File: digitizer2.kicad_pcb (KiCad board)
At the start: 6 copper layers, 75 x 100 mm, 206 parts, among them P1 USB_OTG, P2 CONN_01X01, P3 CONN_01X01, T1 ETC1-1-13, T2 ETC1-1-13, U1 XC7A35T, U10 SN65LVDS100DGK, U11 SN65LVDS100DGK, U2 FT2232H, U3 MT41J128M16, U4 ADS5403, U5 LTC3569, U6 TPS79618DCQ, U7 TPS79633DCQ, U8 93LC46BT-I/OT, U9 LM3671MF-3.3, Y1 12MHz

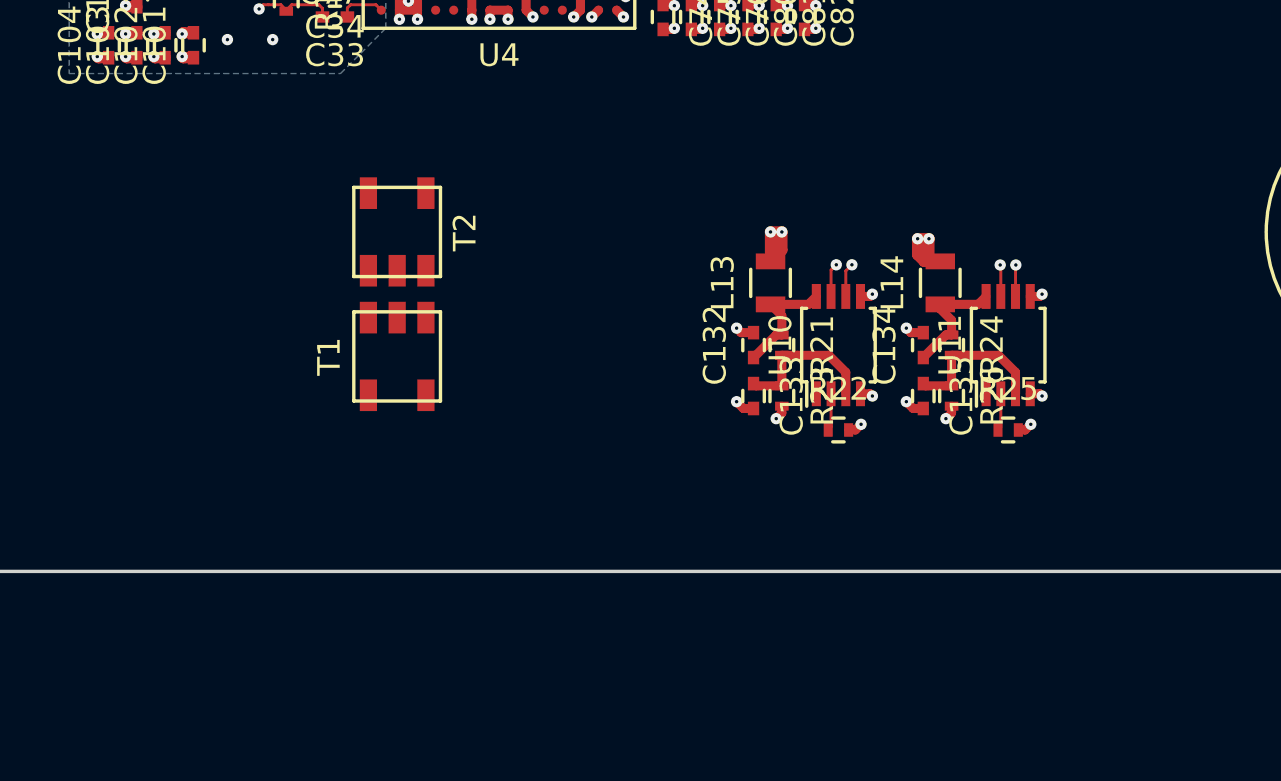
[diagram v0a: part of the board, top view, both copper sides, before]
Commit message: Add SMA connectors
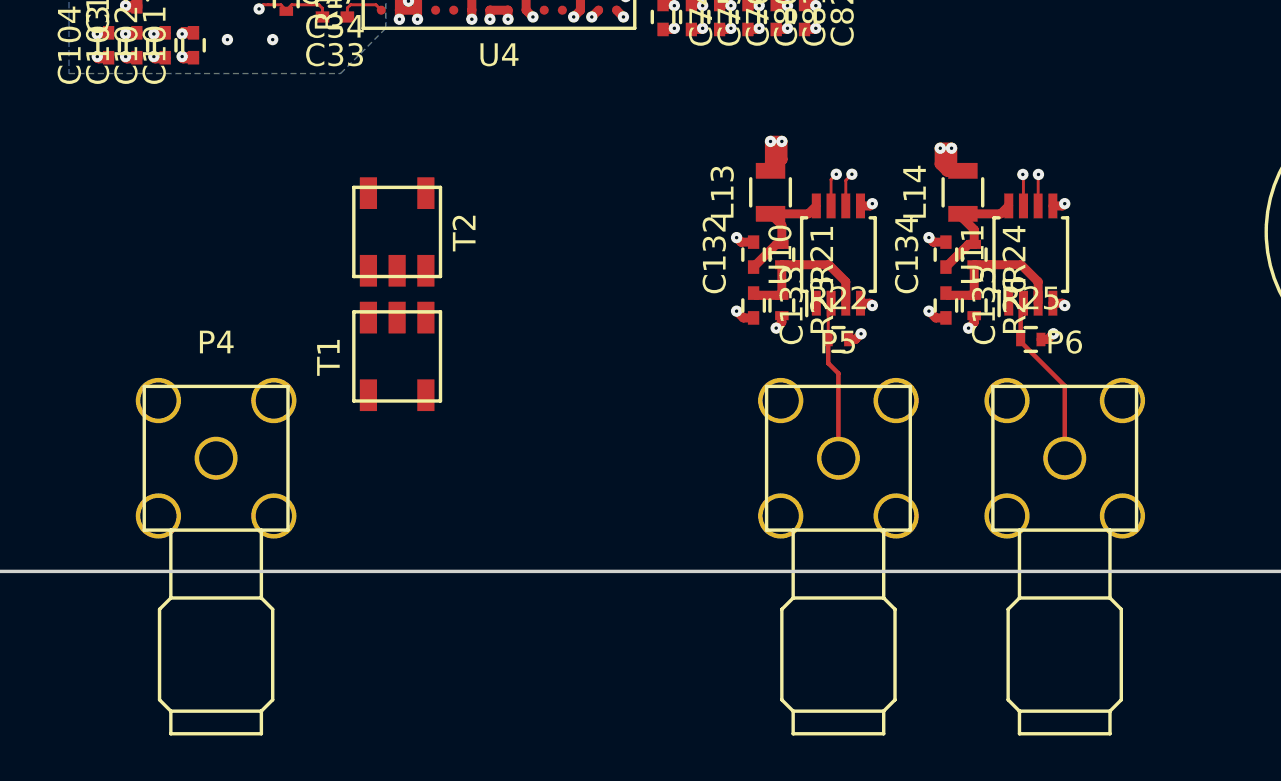
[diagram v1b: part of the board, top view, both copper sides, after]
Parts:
- added P4: SMA, digitizer2_modules:SMA_ANGLE_THT, F.Cu at (147.5, 150.0)
- added P5: SMA, digitizer2_modules:SMA_ANGLE_THT, F.Cu at (175.0, 150.0)
- added P6: SMA, digitizer2_modules:SMA_ANGLE_THT, F.Cu at (185.0, 150.0)
- moved C134 4.12 mm to (179.8, 141.0)
- moved C135 4.12 mm to (179.8, 143.2)
- moved L14 4.12 mm to (180.5, 138.2)
- moved R24 4.12 mm to (181.0, 141.0)
- moved R25 4.12 mm to (183.5, 144.8)
- moved R26 4.12 mm to (181.0, 143.2)
- moved U11 4.12 mm to (183.5, 141.0)
- moved C132 4.00 mm to (171.2, 141.0)
- moved C133 4.00 mm to (171.2, 143.2)
- moved L13 4.00 mm to (172.0, 138.2)
- moved R21 4.00 mm to (172.5, 141.0)
- moved R22 4.00 mm to (175.0, 144.8)
- moved R23 4.00 mm to (172.5, 143.2)
- moved U10 4.00 mm to (175.0, 141.0)
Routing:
- net Net-(P6-Pad1): track 1.65 -> 7.71 mm
- net Net-(P5-Pad1): track 1.65 -> 7.09 mm
- net /DIN2_N: track 51.6 -> 48.0 mm
- net /DIN2_P: track 51.1 -> 48.0 mm
- net /DIN1_P: track 51.0 -> 48.0 mm
- net /DIN1_N: track 51.0 -> 48.0 mm
- net /VDD_ADC_3V3: track 55.6 -> 53.9 mm

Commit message: First digitizer2 release candidate
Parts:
- added C143: 100nF, Capacitors_SMD:C_0402, F.Cu at (140.5, 102.5)
- added C144: 1uF, Capacitors_SMD:C_0402, F.Cu at (158.8, 138.5)
- added C145: 6.8pF NC, Capacitors_SMD:C_0603, F.Cu at (155.0, 152.5)
- added C146: 100nF, Capacitors_SMD:C_0402, F.Cu at (157.5, 138.5)
- added C147: 1uF, Capacitors_SMD:C_0402, F.Cu at (156.2, 138.5)
- added C148: 100nF, Capacitors_SMD:C_0402, F.Cu at (166.0, 133.0)
- added P7: CONN_02X03, Pin_Headers:Pin_Header_Angled_2x03, B.Cu at (140.0, 140.0)
- added P8: CONN_02X03, Pin_Headers:Pin_Header_Angled_2x03, F.Cu at (201.5, 89.5)
- added R29: 0, Resistors_SMD:R_0603, F.Cu at (155.0, 151.0)
- added R30: 0, Resistors_SMD:R_0603, F.Cu at (157.8, 151.0)
- added R31: 50, Resistors_SMD:R_0402, F.Cu at (158.5, 136.8)
- added R32: 0, Resistors_SMD:R_0603, F.Cu at (154.2, 148.5)
- added R33: 50, Resistors_SMD:R_0402, F.Cu at (156.5, 136.8)
- added R34: 100 NC, Resistors_SMD:R_0402, F.Cu at (157.6, 132.0)
- added R35: NC, Resistors_SMD:R_0402, F.Cu at (159.3, 137.9)
- added R36: NC, Resistors_SMD:R_0402, F.Cu at (155.7, 137.9)
- added U12: ASTMLPA-18-100.000MHZ-EJ-E-T, digitizer2_modules:ASTMLPA, F.Cu at (140.5, 100.5)
- moved P5 5.00 mm to (170.0, 150.0)
- moved T2 3.01 mm to (157.5, 142.2)
- moved T1 2.83 mm to (157.5, 147.5)
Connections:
- net /GCLK1_N renamed Net-(U1-PadC4)
- P4 pad 2: Net-(P4-Pad2) -> GND
- U1 pad D4: /GCLK1_P -> /GCLK1
- U1 pad P10: /GCLK2_P -> /GPIO1_P
- U1 pad P11: /GCLK2_N -> /GPIO1_N
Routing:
- net GND: track 242.4 -> 448.9 mm, vias 274 -> 401
- net (no net): track 74.3 -> 0.00 mm, vias 34 -> 0
- net /VDD_ADC_3V3: track 53.9 -> 95.2 mm
- net /GPIO1_N: track 0.00 -> 40.7 mm, vias 0 -> 1
- net /GPIO1_P: track 0.00 -> 40.2 mm, vias 0 -> 1
- net /ADC_VCM: track 0.42 -> 37.2 mm, vias 1 -> 4
- net /INA_BYPASS_P: track 0.00 -> 26.0 mm, vias 0 -> 1
- net /INA_BYPASS_N: track 0.00 -> 25.4 mm, vias 0 -> 1
- net /5V0: track 63.4 -> 38.3 mm
- net /GCLK2_N: track 22.7 -> 0.00 mm, vias 1 -> 0
- net /GCLK2_P: track 22.3 -> 0.00 mm, vias 1 -> 0
- net /GCLK1: track 0.00 -> 16.0 mm, vias 0 -> 2
- net /GCLK1_P: track 12.4 -> 0.00 mm, vias 1 -> 0
- net Net-(U1-PadC4): track 12.4 -> 0.00 mm, vias 1 -> 0
- net /ADC_INA_N: track 0.00 -> 8.35 mm
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- added copper zone on B.Cu, net GND
- added copper zone on In2.Cu, net GND

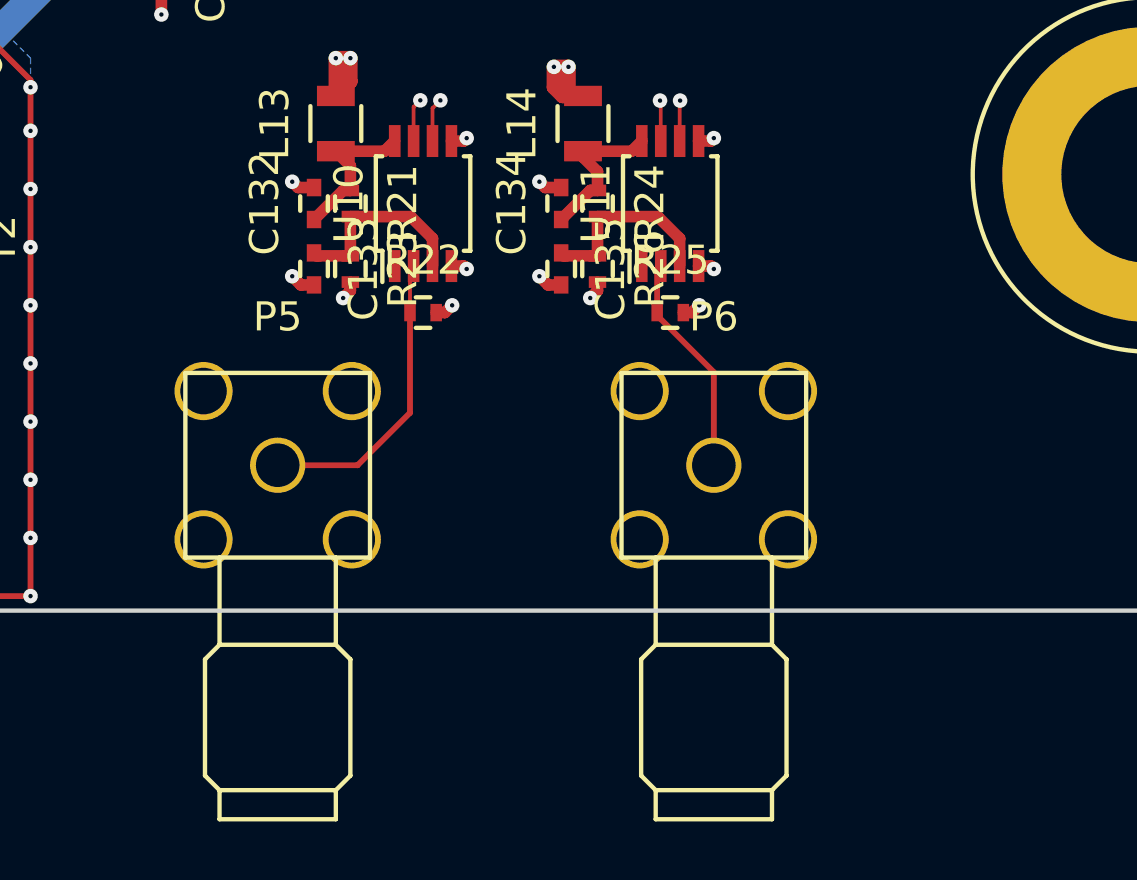
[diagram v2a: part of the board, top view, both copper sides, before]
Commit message: Add pads for input termination
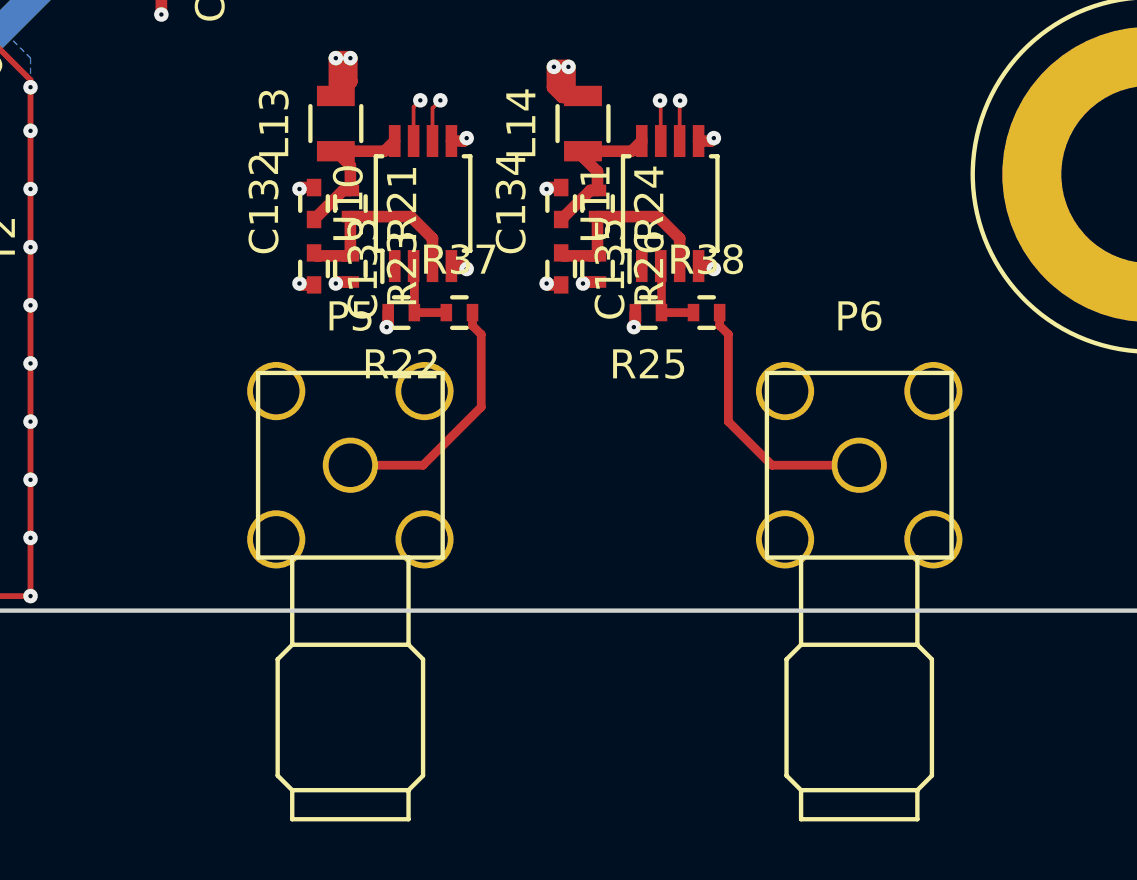
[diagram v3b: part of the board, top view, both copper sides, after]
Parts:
- added R37: 0, Resistors_SMD:R_0402, F.Cu at (176.2, 144.8)
- added R38: 0, Resistors_SMD:R_0402, F.Cu at (184.8, 144.8)
- R31, R33: value 50 -> 25
- moved P6 5.00 mm to (190.0, 150.0)
- moved P5 2.50 mm to (172.5, 150.0)
- moved R22 0.75 mm to (174.2, 144.8), turned to 180 degrees
- moved R25 0.75 mm to (182.8, 144.8), turned to 180 degrees
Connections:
- R22 pad 1: Net-(P5-Pad1) -> Net-(R22-Pad1)
- R25 pad 1: Net-(P6-Pad1) -> Net-(R25-Pad1)
- U10 pad 2: Net-(P5-Pad1) -> Net-(R22-Pad1)
- U11 pad 2: Net-(P6-Pad1) -> Net-(R25-Pad1)
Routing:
- net GND: track 448.9 -> 412.2 mm, vias 401 -> 373
- net (no net): track 0.00 -> 34.9 mm, vias 0 -> 28
- net Net-(R22-Pad1): track 0.00 -> 2.89 mm
- net Net-(R25-Pad1): track 0.00 -> 2.71 mm
- net Net-(P5-Pad1): track 10.4 -> 8.70 mm
- net Net-(P6-Pad1): track 7.71 -> 9.00 mm
